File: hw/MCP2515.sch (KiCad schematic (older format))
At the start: 8 parts, among them U401 MCP2515, U402 MCP2551_SOIC8, X401 XTAL_7A-12.000MAAJ-T

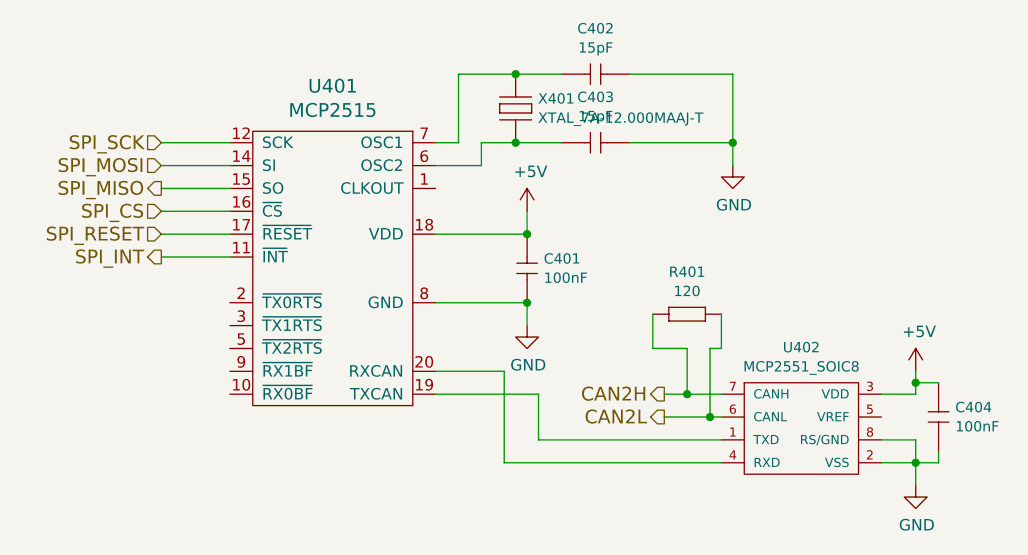
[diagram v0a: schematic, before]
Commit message: tantalum cap added to mcp2515
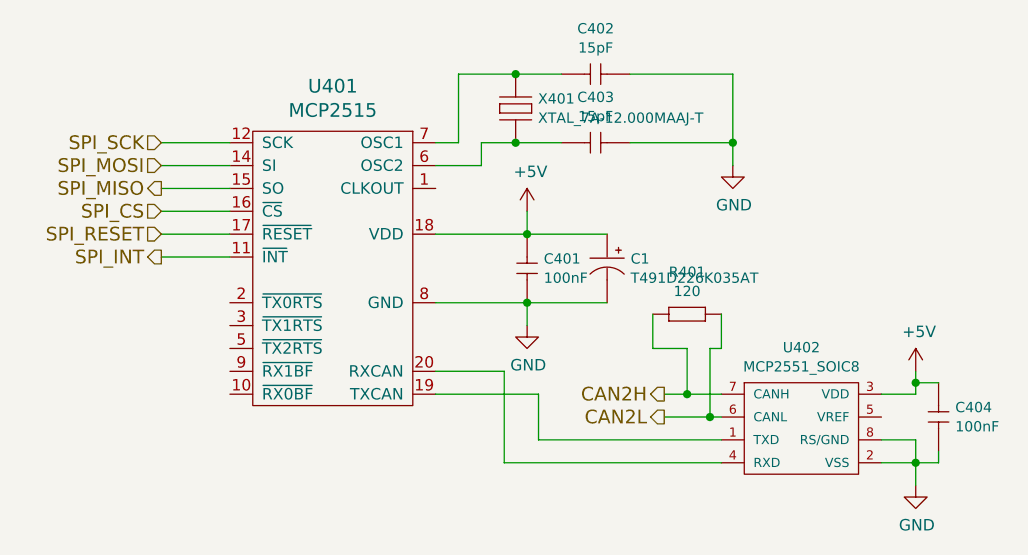
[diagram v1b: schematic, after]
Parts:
- added C1: T491D226K035AT, kemet:7343, symbol kemet:T491D226K035AT
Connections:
- net +5V: now also C1.+
- net GND: now also C1.-
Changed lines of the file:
@@
 Wire Wire Line
 	7400 4100 7300 4100
+Wire Wire Line
+	7050 3400 6700 3400
+Wire Wire Line
+	7050 3700 6700 3700
+$Comp
+L kemet:T491D226K035AT C1
+U 1 1 5BE9F6AC
+P 7050 3600
+F 0 "C1" V 6958 3703 45  0000 L CNN
+F 1 "T491D226K035AT" V 7042 3703 45  0000 L CNN
+F 2 "kemet:7343" H 7080 3750 20  0001 C CNN
+F 3 "http://www.farnell.com/datasheets/2121523.pdf?_ga=1.259966538.1948984246.1460023966" H 7050 3540 60  0001 C CNN
+F 4 "399-8375-1-ND" H 7650 4140 60  0001 C CNN "2nd Source Part Number"
+F 5 "Farnell" H 7350 3840 60  0001 C CNN "1st Source"
+F 6 "T491D226K035AT" H 7250 3740 60  0001 C CNN "Manufacturer Part Number"
+F 7 "Digikey" H 7550 4040 60  0001 C CNN "2nd Source"
+F 8 "Kemet" H 7150 3640 60  0001 C CNN "Manufacturer"
+F 9 "1457504" H 7450 3940 60  0001 C CNN "1st Source Part Number"
+	1    7050 3600
+	0    1    1    0
+$EndComp
 $EndSCHEMATC

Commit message: 1.4.0 pcb created, tantalum caps changed to bigger ones
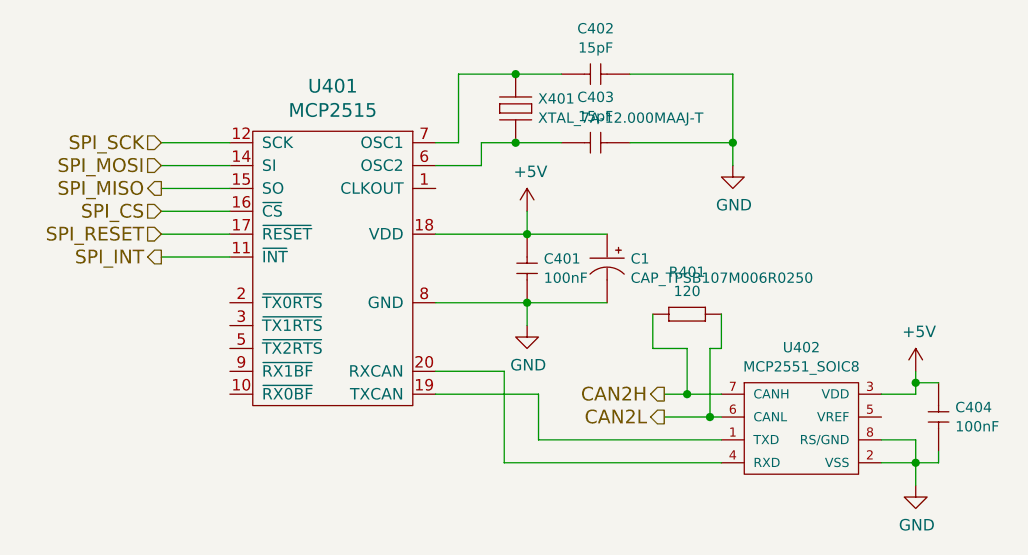
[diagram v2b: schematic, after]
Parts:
- removed C1: T491D226K035AT, kemet:7343, symbol kemet:T491D226K035AT
- added C1: CAP_TPSB107M006R0250, usevolt:1210_CAP, symbol usevolt:CAP_TPSB107M006R0250
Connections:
- net +5V: now also C1.+
- net GND: now also C1.-
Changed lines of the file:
@@
 	7050 3700 6700 3700
 $Comp
-L kemet:T491D226K035AT C1
-U 1 1 5BE9F6AC
+L usevolt:CAP_TPSB107M006R0250 C1
+U 1 1 5C61AE74
 P 7050 3600
 F 0 "C1" V 6958 3703 45  0000 L CNN
-F 1 "T491D226K035AT" V 7042 3703 45  0000 L CNN
-F 2 "kemet:7343" H 7080 3750 20  0001 C CNN
-F 3 "http://www.farnell.com/datasheets/2121523.pdf?_ga=1.259966538.1948984246.1460023966" H 7050 3540 60  0001 C CNN
-F 4 "399-8375-1-ND" H 7650 4140 60  0001 C CNN "2nd Source Part Number"
-F 5 "Farnell" H 7350 3840 60  0001 C CNN "1st Source"
-F 6 "T491D226K035AT" H 7250 3740 60  0001 C CNN "Manufacturer Part Number"
-F 7 "Digikey" H 7550 4040 60  0001 C CNN "2nd Source"
-F 8 "Kemet" H 7150 3640 60  0001 C CNN "Manufacturer"
-F 9 "1457504" H 7450 3940 60  0001 C CNN "1st Source Part Number"
+F 1 "CAP_TPSB107M006R0250" V 7042 3703 45  0000 L CNN
+F 2 "usevolt:1210_CAP" H 7080 3750 20  0001 C CNN
+F 3 "http://datasheets.avx.com/TPS.pdf" H 7050 3540 60  0001 C CNN
+F 4 "AVX Corporation" H 7150 3640 60  0001 C CNN "Manufacturer"
+F 5 "TPSB107M006R0250" H 7250 3740 60  0001 C CNN "Manufacturer Part Number"
+F 6 "Digi-Key" H 7350 3840 60  0001 C CNN "1st Source"
+F 7 "478-4978-1-ND" H 7450 3940 60  0001 C CNN "1st Source Part Number"
+F 8 "Mouser" H 7550 4040 60  0001 C CNN "2nd Source"
+F 9 "581-TPSB107M006R0250" H 7650 4140 60  0001 C CNN "2nd Source Part Number"
 	1    7050 3600
 	0    1    1    0

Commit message: hw 1.5.0, 2 ain inputs added
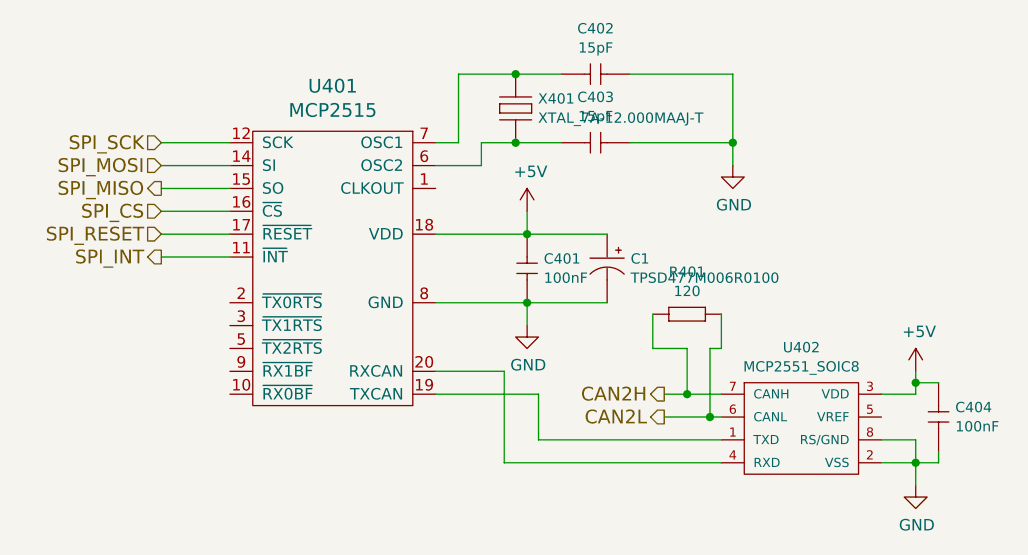
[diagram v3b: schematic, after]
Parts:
- removed C1: CAP_TPSB107M006R0250, usevolt:1210_CAP, symbol usevolt:CAP_TPSB107M006R0250
- added C1: TPSD477M006R0100, usevolt:7343, symbol usevolt:TPSD477M006R0100
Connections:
- net +5V: now also C1.+
- net GND: now also C1.-
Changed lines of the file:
@@
 $Descr A4 11693 8268
 encoding utf-8
-Sheet 4 13
+Sheet 4 14
 Title ""
 Date ""
@@
 	7050 3700 6700 3700
 $Comp
-L usevolt:CAP_TPSB107M006R0250 C1
-U 1 1 5C61AE74
+L usevolt:TPSD477M006R0100 C1
+U 1 1 5D37AB73
 P 7050 3600
 F 0 "C1" V 6958 3703 45  0000 L CNN
-F 1 "CAP_TPSB107M006R0250" V 7042 3703 45  0000 L CNN
-F 2 "usevolt:1210_CAP" H 7080 3750 20  0001 C CNN
+F 1 "TPSD477M006R0100" V 7042 3703 45  0000 L CNN
+F 2 "usevolt:7343" H 7080 3750 20  0001 C CNN
 F 3 "http://datasheets.avx.com/TPS.pdf" H 7050 3540 60  0001 C CNN
-F 4 "AVX Corporation" H 7150 3640 60  0001 C CNN "Manufacturer"
-F 5 "TPSB107M006R0250" H 7250 3740 60  0001 C CNN "Manufacturer Part Number"
-F 6 "Digi-Key" H 7350 3840 60  0001 C CNN "1st Source"
-F 7 "478-4978-1-ND" H 7450 3940 60  0001 C CNN "1st Source Part Number"
-F 8 "Mouser" H 7550 4040 60  0001 C CNN "2nd Source"
-F 9 "581-TPSB107M006R0250" H 7650 4140 60  0001 C CNN "2nd Source Part Number"
+F 4 "478-1790-1-ND" H 7650 4140 60  0001 C CNN "2nd Source Part Number"
+F 5 "Farnell" H 7350 3840 60  0001 C CNN "1st Source"
+F 6 "TPSD477M006R0100" H 7250 3740 60  0001 C CNN "Manufacturer Part Number"
+F 7 "Digikey" H 7550 4040 60  0001 C CNN "2nd Source"
+F 8 "AVX Corporation" H 7150 3640 60  0001 C CNN "Manufacturer"
+F 9 "2852793" H 7450 3940 60  0001 C CNN "1st Source Part Number"
 	1    7050 3600
 	0    1    1    0
